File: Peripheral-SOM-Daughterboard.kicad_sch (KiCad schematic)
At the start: 3 parts, among them J1 Conn_02x10_Odd_Even

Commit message: more naming...
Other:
- note added: "Daughterboard Features"
- note removed: "Boot Features"
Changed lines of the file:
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@@
     (effects (font (size 1.27 1.27)) (justify left bottom))
   )
-  (text "Boot Features" (at 12.7 16.51 0)
+  (text "Daughterboard Features" (at 12.7 16.51 0)
     (effects (font (size 2.54 2.54) (thickness 0.508) bold) (justify left bottom))
   )

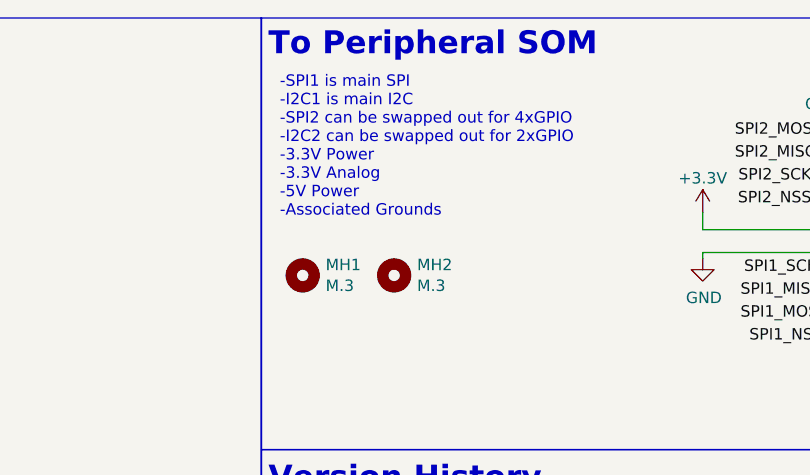
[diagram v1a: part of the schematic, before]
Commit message: Updated template for new SOM pinout + added lck and backups to gitignore
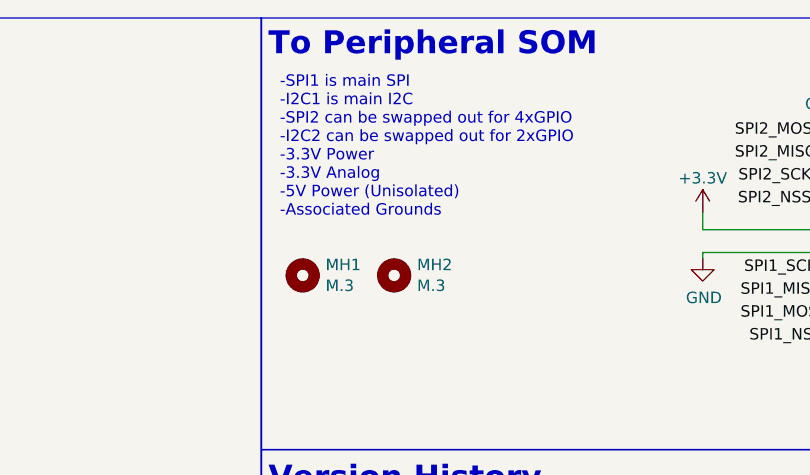
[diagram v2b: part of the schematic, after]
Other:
- note added: "-SPI1 is main SPI -I2C1 is main I2C -SPI2 can be swapped out for 4xGPIO -I2C2 can be swapped out for 2xGPIO -3.3V Power -3.3V Analog -5V Power (Unisolated) -Associated Grounds"
- note removed: "-SPI1 is main SPI -I2C1 is main I2C -SPI2 can be swapped out for 4xGPIO -I2C2 can be swapped out for 2xGPIO -3.3V Power -3.3V Analog -5V Power -Associated Grounds"
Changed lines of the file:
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@@
     (effects (font (size 2.54 2.54) (thickness 0.508) bold) (justify left bottom))
   )
-  (text "-SPI1 is main SPI\n-I2C1 is main I2C\n-SPI2 can be swapped out for 4xGPIO\n-I2C2 can be swapped out for 2xGPIO\n-3.3V Power\n-3.3V Analog\n-5V Power\n-Associated Grounds"
+  (text "-SPI1 is main SPI\n-I2C1 is main I2C\n-SPI2 can be swapped out for 4xGPIO\n-I2C2 can be swapped out for 2xGPIO\n-3.3V Power\n-3.3V Analog\n-5V Power (Unisolated)\n-Associated Grounds"
     (at 179.07 34.29 0)
     (effects (font (size 1.27 1.27)) (justify left bottom))
